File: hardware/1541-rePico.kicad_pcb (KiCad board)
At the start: 2 copper layers, 59.1 x 60 mm, 14 parts, among them IC2 VIA6522, J1 Display Connector, J2 Conn_02x03_Odd_Even, J3 RESET_1541, J4 SD Card Module Connector, J5 EXT_5V, P1 VIA_PIN_1-20, P2 VIA_PIN_21-40, SW1 RESET, U1 Pico

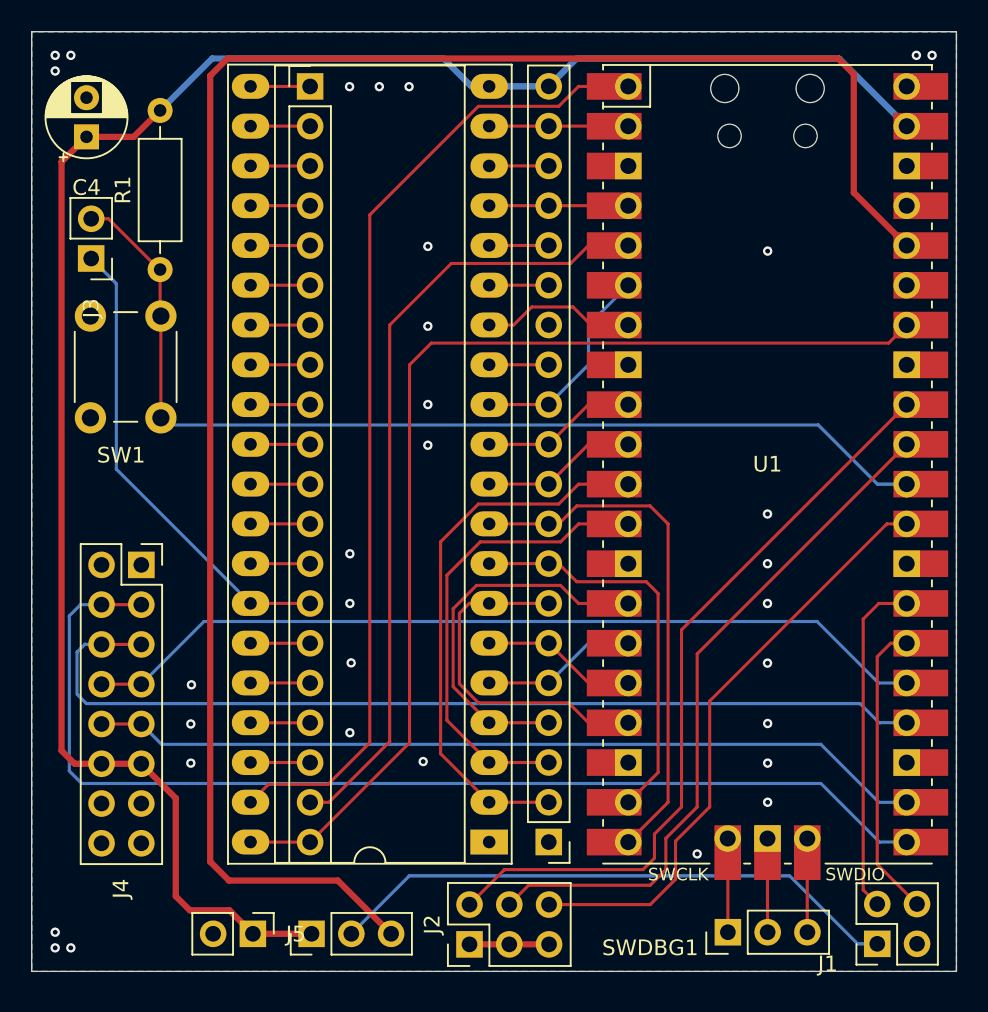
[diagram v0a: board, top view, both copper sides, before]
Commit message: new PCB layout + BRDY fix
changed rotary-encoder connector to default 5 pin
flipped BRDY signal (GPIO28) with BT3 (GPIO22) to
 not violate 5V tollerance of GPIO28.
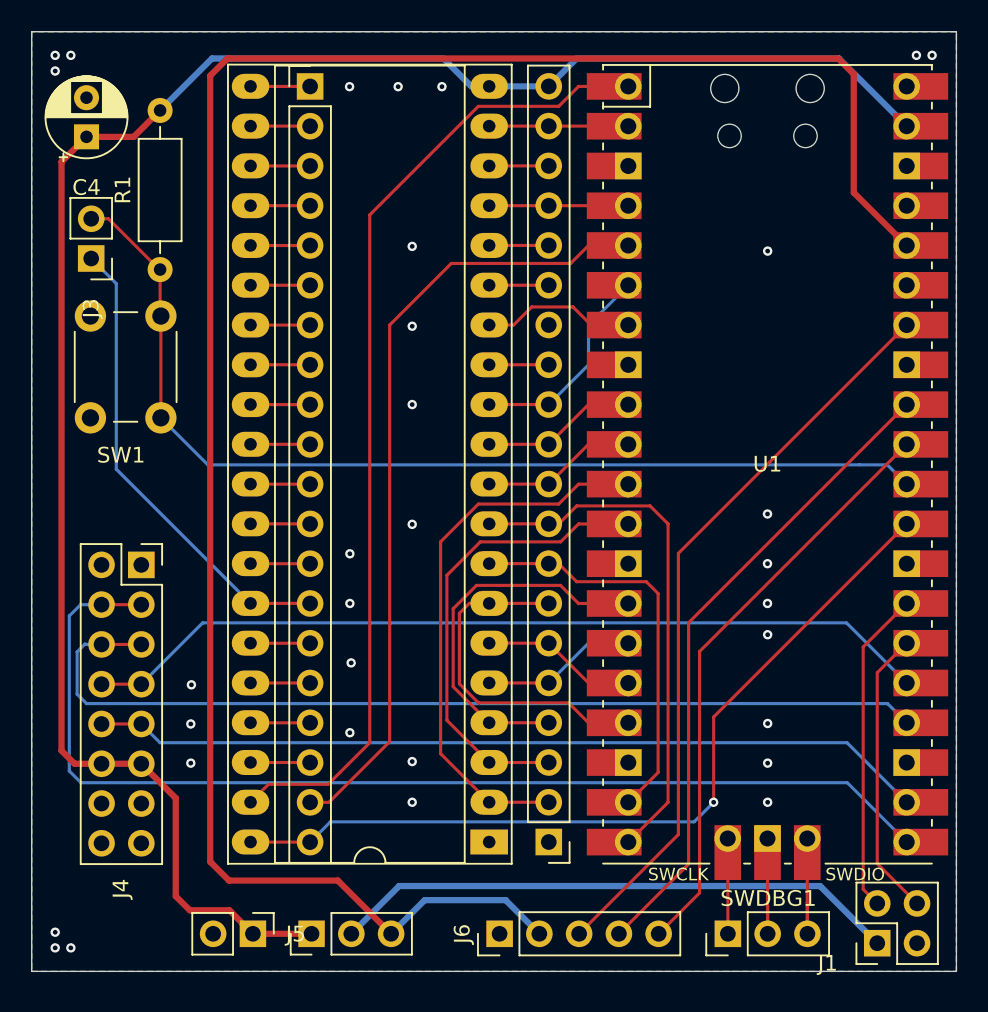
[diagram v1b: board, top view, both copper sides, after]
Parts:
- removed J2: Conn_02x03_Odd_Even, Connector_PinHeader_2.54mm:PinHeader_2x03_P2.54mm_Vertical
- added J6: Conn_01x05_Pin, Connector_PinHeader_2.54mm:PinHeader_1x05_P2.54mm_Vertical, F.Cu at (130.1, 122.7)
- moved SWDBG1 0.10 mm to (144.6, 122.7)
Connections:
- U1 pad 29: /BT3 -> /VIA 6522 Sockel/BRDY
- U1 pad 31: /BT2 -> Net-(J6-Pin_5)
- U1 pad 32: /BT1 -> Net-(J6-Pin_4)
- U1 pad 34: /VIA 6522 Sockel/BRDY -> Net-(J6-Pin_3)
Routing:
- net /BT1: track 48.7 -> 0.00 mm
- net Net-(J6-Pin_3): track 0.00 -> 47.5 mm
- net /BT2: track 44.5 -> 0.00 mm
- net Net-(J6-Pin_4): track 0.00 -> 41.4 mm
- net /BT3: track 38.3 -> 0.00 mm
- net Net-(J6-Pin_5): track 0.00 -> 37.8 mm
- net /VIA 6522 Sockel/BRDY: track 69.7 -> 53.5 mm, vias 0 -> 1
- net +3.3V: track 118.0 -> 129.2 mm
- net GND: track 5.08 -> 0.00 mm
- net Net-(SWDBG1-Pin_3): track 5.99 -> 7.99 mm
- net Net-(SWDBG1-Pin_2): track 5.99 -> 7.74 mm
- net I2C_SCL: track 21.8 -> 20.7 mm
- net I2C_SDA: track 19.1 -> 18.4 mm
- net Net-(Display_Power1-Pin_2): track 36.9 -> 36.4 mm

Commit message: new PCB layout to support WPS external
invert WPS signal to be used as input of photo-sensor
circuit of 1541-main pcb.
avoids the concurrent access of the WPS signal between
GateArray and VIA - now this comes from 74LS04
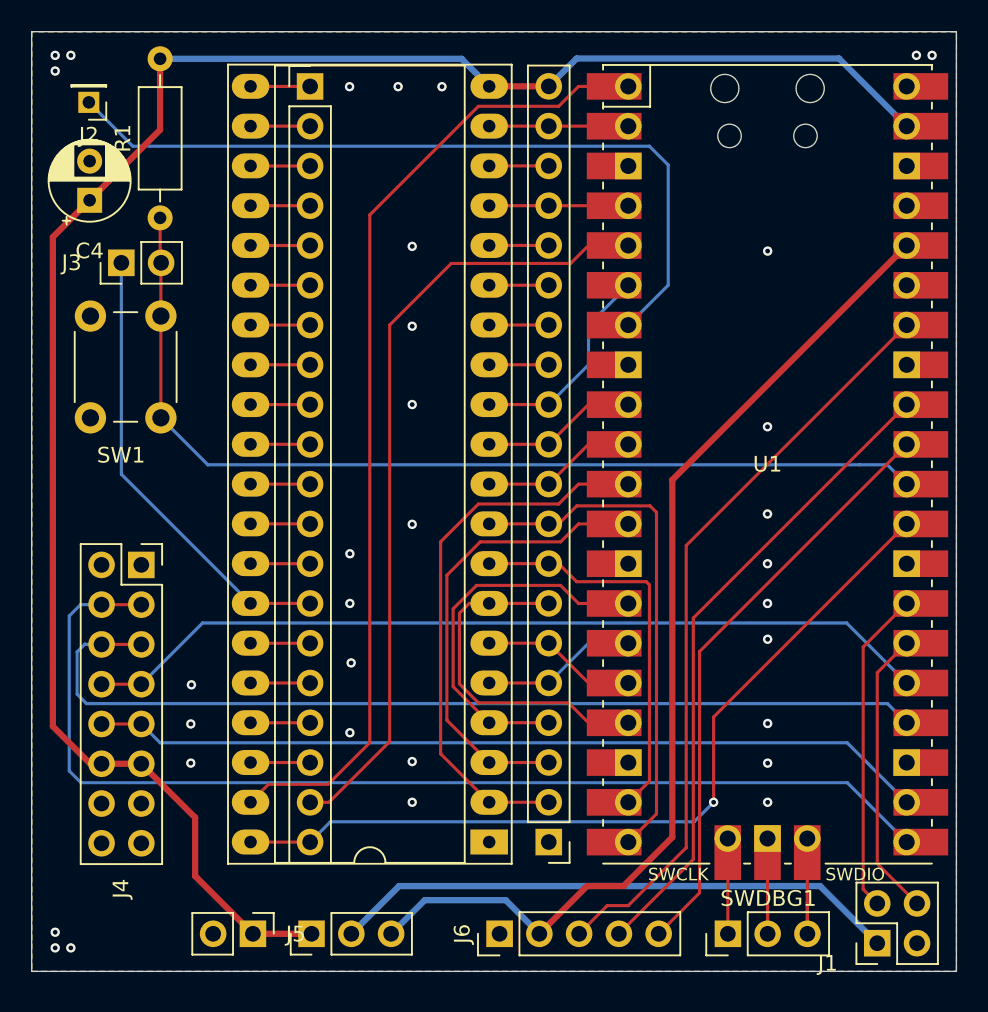
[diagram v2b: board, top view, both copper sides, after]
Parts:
- added J2: Conn_01x01_Pin, Connector_PinHeader_2.00mm:PinHeader_1x01_P2.00mm_Vertical, F.Cu at (103.8, 69.6)
- moved C4 4.05 mm to (103.9, 75.8)
- moved R1 3.30 mm to (108.4, 76.9)
- moved J3 1.94 mm to (105.9, 79.8), turned to 90 degrees
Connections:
- P1 pad 14: unconnected-(P1-Pin_14-Pad14) -> /VIA 6522 Sockel/WPS
- U1 pad 7: /VIA 6522 Sockel/WPS -> Net-(J2-Pin_1)
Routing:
- net +3.3V: track 129.2 -> 66.3 mm
- net Net-(J2-Pin_1): track 0.00 -> 49.9 mm
- net /VIA 6522 Sockel/WPS: track 9.85 -> 3.81 mm
- net Net-(J3-Pin_2): track 64.6 -> 62.3 mm
- net +5V: track 122.2 -> 120.6 mm
- net /VIA 6522 Sockel/~{RESET}: track 30.0 -> 29.0 mm
- net Net-(J6-Pin_3): track 47.5 -> 48.3 mm
- net /VIA 6522 Sockel/PA7: track 33.7 -> 33.1 mm
- net GND: vias 32 -> 33

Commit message: updated kicad-files for gerber creation
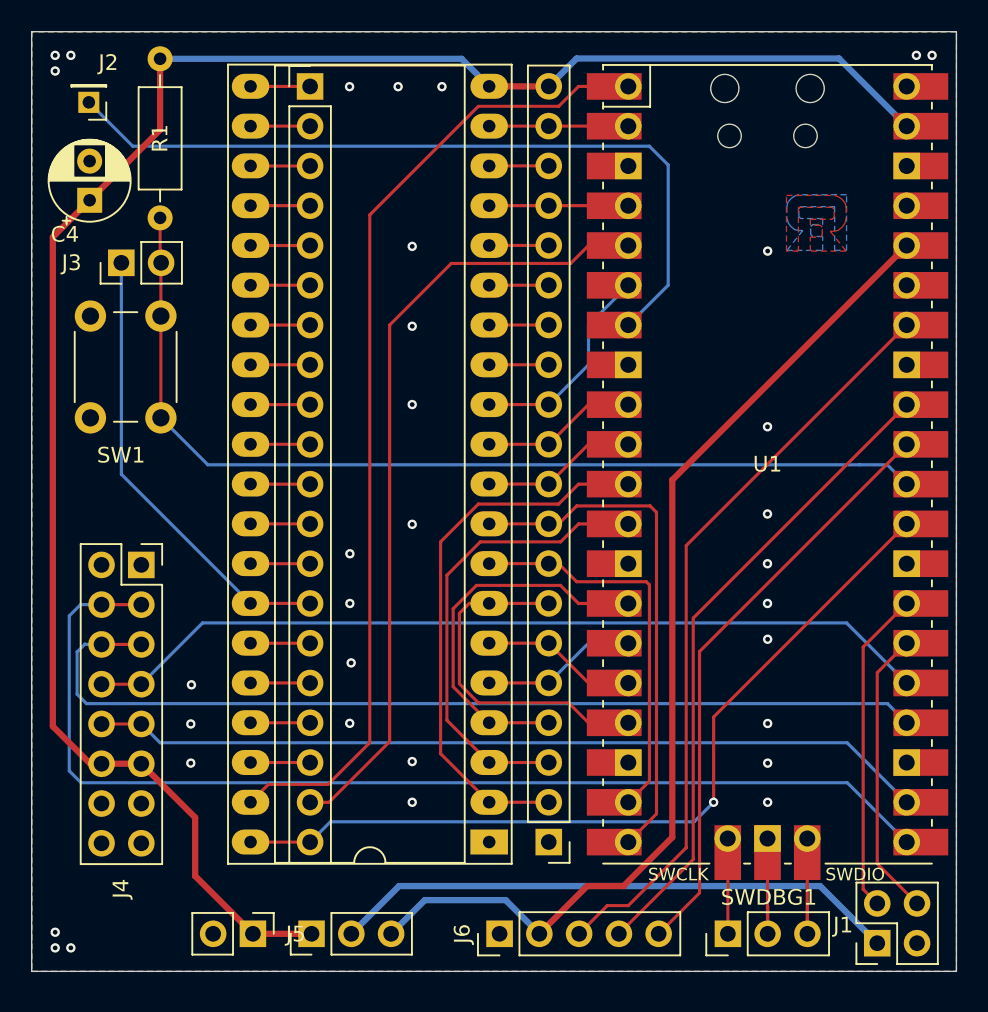
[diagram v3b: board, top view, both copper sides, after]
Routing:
- added copper zone on B.Cu, net (none)
- added copper zone on F.Cu, net (none)
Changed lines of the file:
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@@
 			(disableapertmacros no)
 			(usegerberextensions no)
-			(usegerberattributes yes)
+			(usegerberattributes no)
 			(usegerberadvancedattributes yes)
 			(creategerberjobfile yes)
@@
 			(plotframeref no)
 			(mode 1)
-			(useauxorigin no)
+			(useauxorigin yes)
 			(hpglpennumber 1)
 			(hpglpenspeed 20)
@@
 			(outputformat 1)
 			(mirror no)
-			(drillshape 1)
+			(drillshape 0)
 			(scaleselection 1)
-			(outputdirectory "")
+			(outputdirectory "./CAM")
 		)
 	)
@@
 		(tags "Resistor Axial_DIN0207 series Axial Horizontal pin pitch 10.16mm 0.25W = 1/4W length 6.3mm diameter 2.5mm")
 		(property "Reference" "R1"
-			(at 5.08 -2.37 90)
+			(at 5.08 0 90)
 			(layer "F.SilkS")
 			(effects
@@
 		(tags "CP Radial series Radial pin pitch 2.50mm  diameter 5mm Electrolytic Capacitor")
 		(property "Reference" "C4"
-			(at -3.239887 0 0)
+			(at -2.184887 -1.58 0)
 			(layer "F.SilkS")
 			(effects
@@
 		(tags "Through hole pin header THT 1x01 2.00mm single row")
 		(property "Reference" "J2"
-			(at 0 -2.11 0)
+			(at -1.25 2.53 0)
 			(layer "F.SilkS")
 			(effects
@@
 			(at 0 2.11 0)
 			(layer "F.Fab")
+			(hide yes)
 			(effects
 				(font
@@
 		)
 		(fp_text user "${REFERENCE}"
-			(at 7.62 24.13 0)
+			(at 5.455 -0.15 0)
 			(layer "F.Fab")
 			(effects
@@
 			(at -1.905 -6.35 0)
 			(layer "F.Fab")
+			(hide yes)
 			(effects
 				(font
@@
 		(tags "Through hole socket strip THT 2x02 2.54mm double row")
 		(property "Reference" "J1"
-			(at 3.155 -1.29 0)
+			(at 2.18 1.15 0)
 			(layer "F.SilkS")
 			(effects
@@
 		(tags "Through hole pin header THT 1x03 2.54mm single row")
 		(property "Reference" "SWDBG1"
-			(at 2.25 2.59 180)
+			(at 2.32 2.62 180)
 			(layer "F.SilkS")
 			(effects
@@
 	)
 	(via
-		(at 120.4976 109.8296)
+		(at 120.4876 109.2296)
 		(size 0.6)
 		(drill 0.3)
@@
 	)
 	(zone
+		(net 0)
+		(net_name "")
+		(layer "F.Cu")
+		(hatch edge 0.508)
+		(priority 1)
+		(connect_pads
+			(clearance 0.508)
+		)
+		(min_thickness 0.0508)
+		(filled_areas_thickness no)
+		(fill yes
+			(thermal_gap 0.508)
+			(thermal_bridge_width 0.508)
+		)
+		(polygon
+			(pts
+				(xy 151.6796 75.5898) (xy 151.9336 75.7676) (xy 152.1368 76.0216) (xy 152.1876 76.2756) (xy 152.1876 77.0122)
+				(xy 152.1114 77.2916) (xy 151.9336 77.5456) (xy 151.6796 77.7488) (xy 151.4256 77.7996) (xy 151.1716 77.7996)
+				(xy 152.1876 79.0696) (xy 149.9016 79.0696) (xy 149.9016 78.1806) (xy 150.5366 78.1806) (xy 150.6636 78.0536)
+				(xy 150.6636 77.5456) (xy 150.5366 77.4186) (xy 149.9016 77.4186) (xy 149.9016 77.0376) (xy 151.2986 77.0376)
+				(xy 151.4256 76.9106) (xy 151.4256 76.4026) (xy 151.2986 76.2756) (xy 149.1396 76.2756) (xy 149.1396 79.0696)
+				(xy 148.3776 79.0696) (xy 148.3776 75.5136) (xy 151.4256 75.5136)
+			)
+		)
+	)
+	(zone
 		(net 2)
 		(net_name "GND")
@@
 			)
 		)
+	)
+	(zone
+		(net 0)
+		(net_name "")
+		(layer "B.Cu")
+		(hatch edge 0.508)
+		(priority 1)
+		(connect_pads
+			(clearance 0.508)
+		)
+		(min_thickness 0.0508)
+		(filled_areas_thickness no)
+		(fill yes
+			(thermal_gap 0.508)
+			(thermal_bridge_width 0.508)
+		)
+		(polygon
+			(pts
+				(xy 148.9136 75.5458) (xy 148.6596 75.7236) (xy 148.4564 75.9776) (xy 148.4056 76.2316) (xy 148.4056 76.9682)
+				(xy 148.4818 77.2476) (xy 148.6596 77.5016) (xy 148.9136 77.7048) (xy 149.1676 77.7556) (xy 149.4216 77.7556)
+				(xy 148.4056 79.0256) (xy 150.6916 79.0256) (xy 150.6916 78.1366) (xy 150.0566 78.1366) (xy 149.9296 78.0096)
+				(xy 149.9296 77.5016) (xy 150.0566 77.3746) (xy 150.6916 77.3746) (xy 150.6916 76.9936) (xy 149.2946 76.9936)
+				(xy 149.1676 76.8666) (xy 149.1676 76.3586) (xy 149.2946 76.2316) (xy 151.4536 76.2316) (xy 151.4536 79.0256)
+				(xy 152.2156 79.0256) (xy 152.2156 75.4696) (xy 149.1676 75.4696)
+			)
+		)

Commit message: new PCB version 1.5
- added levelshifter ics txs0108epwr between pico and via pins
- added pullup-resistors for I2C (populate if necessary)
- aligned footprint of jumper-headers on 50mil grid
- added version-text and URL on backside
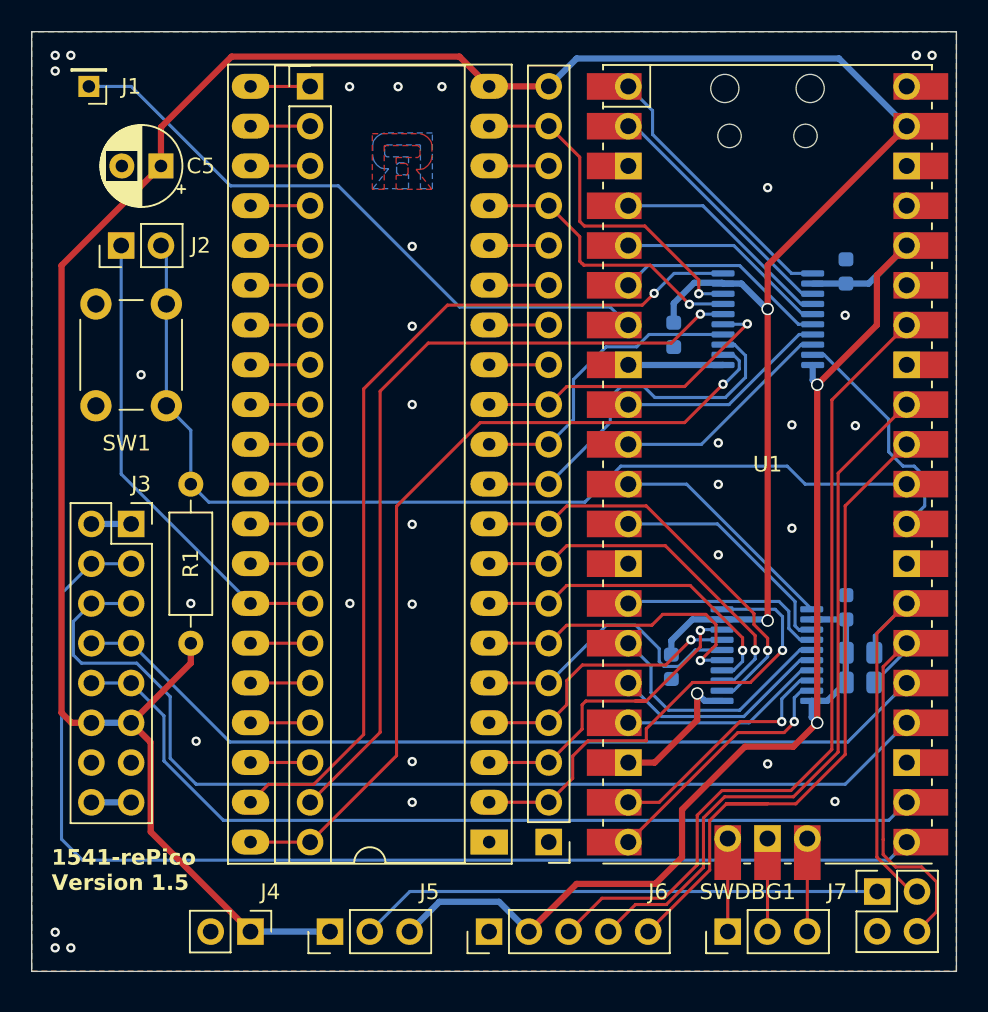
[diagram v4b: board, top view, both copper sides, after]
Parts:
- removed the J3 at (105.9, 79.8)
- added C1: 0,1µF, Capacitor_SMD:C_0603_1608Metric, B.Cu at (141.2, 84.4)
- added C2: 0,1µF, Capacitor_SMD:C_0603_1608Metric, B.Cu at (152.2, 80.4)
- added C3: 0,1µF, Capacitor_SMD:C_0603_1608Metric, B.Cu at (141.0, 105.6)
- added C4: 0,1µF, Capacitor_SMD:C_0603_1608Metric, B.Cu at (152.2, 101.8)
- added J5: Display Power, Connector_PinHeader_2.54mm:PinHeader_1x03_P2.54mm_Vertical, F.Cu at (119.2, 122.5)
- added R2: 1.8k, Resistor_SMD:R_0805_2012Metric, B.Cu at (153.1, 104.7)
- added R3: 1.8k, Resistor_SMD:R_0805_2012Metric, B.Cu at (153.1, 106.6)
- added U2: TXS0108EPW, Package_SO:TSSOP-20_4.4x6.5mm_P0.65mm, B.Cu at (147.1, 104.9)
- added U3: TXS0108EPW, Package_SO:TSSOP-20_4.4x6.5mm_P0.65mm, B.Cu at (147.2, 83.4)
- J2: renamed from Display_Power1; value Display Power -> RESET_1541; footprint Connector_PinHeader_2.54mm:PinHeader_1x03_P2.54mm_Vertical -> Connector_PinHeader_2.54mm:PinHeader_1x02_P2.54mm_Vertical
- moved J2 45.6 mm to (105.9, 78.7)
- moved R1 17.1 mm to (110.3, 94.0), turned to -90 degrees
- moved C5 5.05 mm to (108.4, 73.6), turned to 180 degrees
- moved J7 3.30 mm to (154.2, 120.0), turned to 90 degrees
- moved J3 2.69 mm to (106.5, 96.5)
- moved J1 1.02 mm to (103.8, 68.6)
- moved SW1 0.85 mm to (104.3, 88.9)
- moved J6 0.68 mm to (129.4, 122.5)
- moved J4 0.21 mm to (114.1, 122.5)
- moved SWDBG1 0.14 mm to (144.6, 122.5)
- renumbered C4 to C5, J2 to J1, J4 to J3, J5 to J4, J1 to J7
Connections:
- J2 pad 1: +5V -> /VIA 6522 Sockel/~{RESET}
- J2 pad 2: Net-(Display_Power1-Pin_2) -> Net-(J2-Pin_2)
- J7 pad 1: Net-(Display_Power1-Pin_2) -> Net-(J5-Pin_2)
- R1 pad 1: Net-(J3-Pin_2) -> Net-(J2-Pin_2)
- SW1 pad 2: Net-(J3-Pin_2) -> Net-(J2-Pin_2)
- U1 pad 1: /VIA 6522 Sockel/SOE -> /_SOE
- U1 pad 10: /VIA 6522 Sockel/STP1 -> /_STP1
- U1 pad 11: /VIA 6522 Sockel/PA0 -> /_PA0
- U1 pad 12: /VIA 6522 Sockel/PA1 -> /_PA1
- U1 pad 14: /VIA 6522 Sockel/PA2 -> /_PA2
- U1 pad 15: /VIA 6522 Sockel/PA3 -> /_PA3
- U1 pad 16: /VIA 6522 Sockel/PA4 -> /_PA4
- U1 pad 17: /VIA 6522 Sockel/PA5 -> /_PA5
- U1 pad 19: /VIA 6522 Sockel/PA6 -> /_PA6
- U1 pad 2: /VIA 6522 Sockel/MODE -> /_OE
- U1 pad 20: /VIA 6522 Sockel/PA7 -> /_PA7
- U1 pad 29: /VIA 6522 Sockel/BRDY -> /_BRDY
- U1 pad 30: Net-(J3-Pin_2) -> Net-(J2-Pin_2)
- U1 pad 4: /VIA 6522 Sockel/SYNC -> /_SYNC
- U1 pad 5: /VIA 6522 Sockel/SOE_GA -> /_SOE_GA
- U1 pad 6: /VIA 6522 Sockel/MTR -> /_MTR
- U1 pad 9: /VIA 6522 Sockel/STP0 -> /_STP0
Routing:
- net Net-(J2-Pin_2): track 0.00 -> 64.1 mm
- net Net-(J3-Pin_2): track 62.3 -> 0.00 mm
- net +5V: track 120.6 -> 177.1 mm, vias 0 -> 2
- net Net-(Display_Power1-Pin_2): track 36.4 -> 0.00 mm
- net Net-(J5-Pin_2): track 0.00 -> 33.5 mm
- net +3.3V: track 66.3 -> 86.6 mm, vias 0 -> 2
- net GND: track 0.00 -> 20.3 mm
- net /_SOE: track 0.00 -> 17.6 mm
- net /_PA7: track 0.00 -> 16.6 mm, vias 0 -> 1
- net /_OE: track 0.00 -> 16.2 mm
- net /_PA3: track 0.00 -> 16.1 mm
- net /_PA6: track 0.00 -> 15.8 mm, vias 0 -> 1
- net /_PA1: track 0.00 -> 15.5 mm
- net /_BRDY: track 0.00 -> 15.1 mm
- net /_PA0: track 0.00 -> 15.0 mm
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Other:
- board text added: "1541-rePico Version 1.5"
- board text added: "https://github.com/fook42/1541-repico"

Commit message: minor updates to pcb
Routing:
- net GND: vias 33 -> 32
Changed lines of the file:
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@@
 	)
 	(via
-		(at 144.0276 98.4696)
+		(at 144.6776 99.0696)
 		(size 0.6)
 		(drill 0.3)
@@
 	)
 	(via
-		(at 144.0276 91.3196)
+		(at 144.6776 91.3196)
 		(size 0.6)
 		(drill 0.3)
@@
 	)
 	(via
-		(at 144.0276 93.9696)
+		(at 144.6776 93.9696)
 		(size 0.6)
 		(drill 0.3)
@@
 	)
 	(via
-		(at 148.7276 96.7696)
+		(at 148.7276 99.0696)
 		(size 0.6)
 		(drill 0.3)
@@
 		(size 0.6)
 		(drill 0.3)
-		(layers "F.Cu" "B.Cu")
-		(free yes)
-		(net 2)
-	)
-	(via
-		(at 148.7276 90.1696)
-		(size 0.6)
-		(drill 0.3)
